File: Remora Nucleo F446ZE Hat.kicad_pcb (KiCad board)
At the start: 2 copper layers, 108.2 x 137.1 mm, 30 parts, among them J1 NucleoF446ZE CN11 Header, J10 B_STEP_AND_DIR+-, J11 C_STEP_AND_DIR+-, J12 DIGITAL_OUTPUTS, J14 Digital Inputs, J2 NucleoF446ZE CN12 Header, J3 UART_TX, J4 MSD-1-A, J6 X_STEP_AND_DIR+-, J7 Y_STEP_AND_DIR+-, J8 Z_STEP_AND_DIR+-, J9 A_STEP_AND_DIR+-, SW2 SW_Push

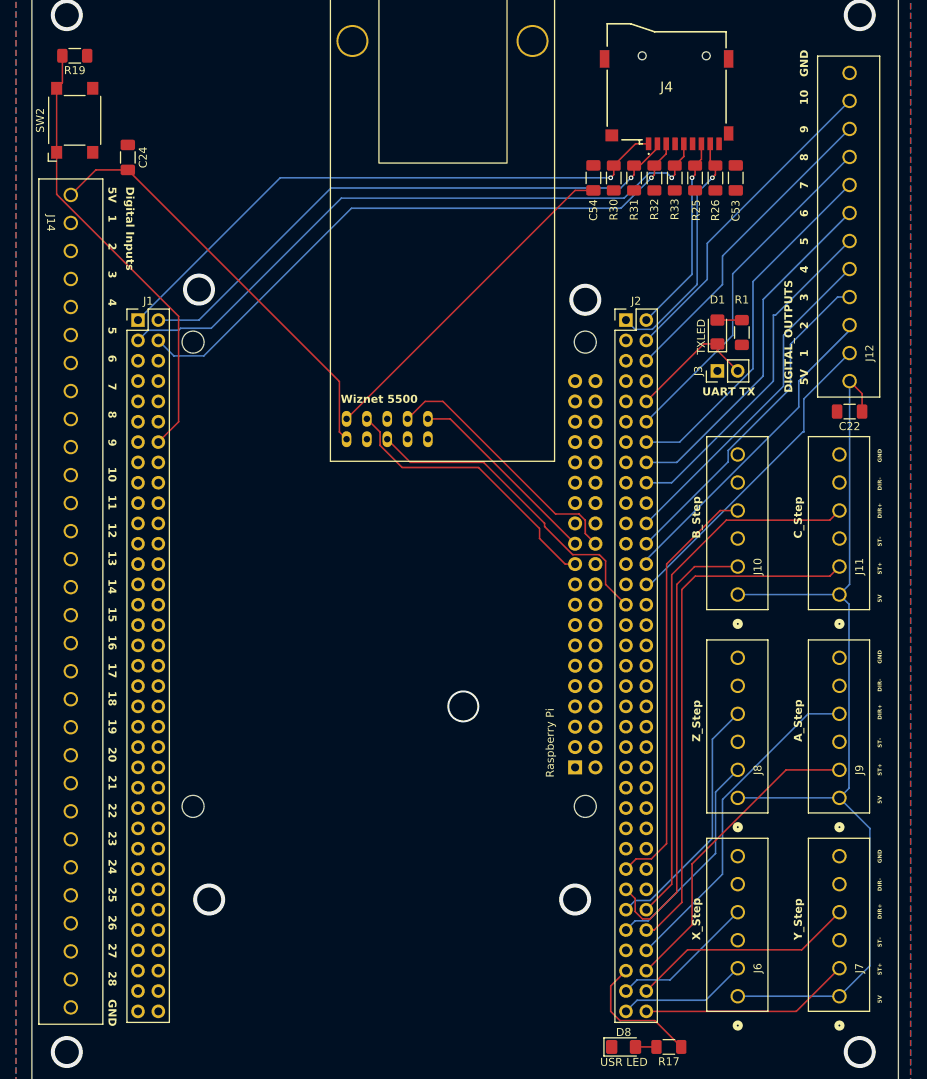
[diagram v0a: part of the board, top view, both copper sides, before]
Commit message: Dropped number of IO on design to make more room. Created the new footprints to suit them, updates to BOM and ran some traces on the PCB.
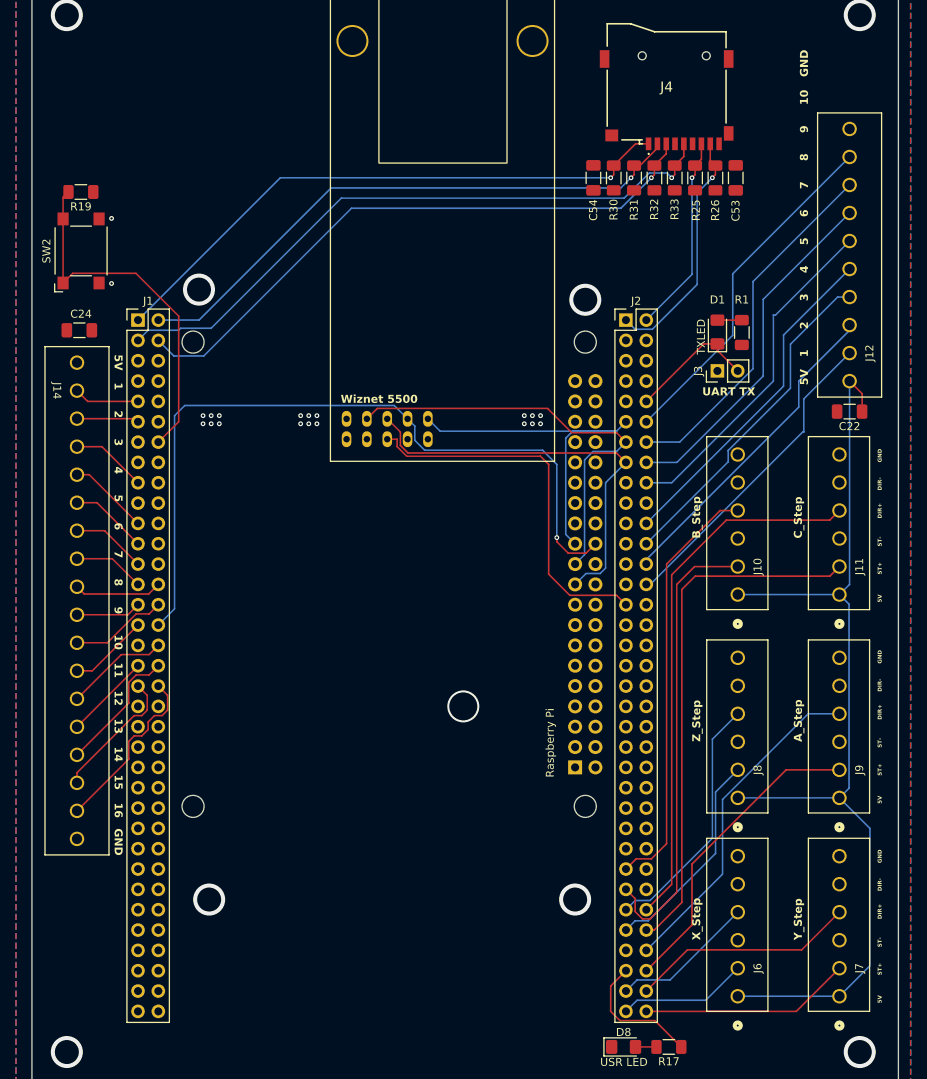
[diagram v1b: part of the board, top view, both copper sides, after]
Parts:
- J12: footprint EBWA_06_A:CONN_EBWA-12-A_ADM -> EBWA_06_A:CONN_EBWA-10-A_ADM
- J14: footprint EBWA_06_A:CONN_EBWA-30-A_ADM -> EBWA_06_A:CONN_EBWA-18-A_ADM
- moved C24 22.4 mm to (99.4, 67.3), turned to 0 degrees
- moved J14 21.0 mm to (99.1, 71.4)
- moved R19 17.0 mm to (99.5, 50.0)
- moved SW2 16.3 mm to (99.6, 57.4)
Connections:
- J1 pad 39: MCU_DIGITAL_IN_17 -> unconnected-(J1-Pin_39-Pad39)
- J1 pad 40: MCU_DIGITAL_IN_18 -> unconnected-(J1-Pin_40-Pad40)
- J1 pad 41: MCU_DIGITAL_IN_19 -> unconnected-(J1-Pin_41-Pad41)
- J1 pad 42: MCU_DIGITAL_IN_20 -> unconnected-(J1-Pin_42-Pad42)
- J1 pad 43: MCU_DIGITAL_IN_21 -> unconnected-(J1-Pin_43-Pad43)
- J1 pad 44: MCU_DIGITAL_IN_22 -> unconnected-(J1-Pin_44-Pad44)
- J1 pad 45: MCU_DIGITAL_IN_23 -> unconnected-(J1-Pin_45-Pad45)
- J1 pad 46: MCU_DIGITAL_IN_24 -> unconnected-(J1-Pin_46-Pad46)
- J1 pad 47: MCU_DIGITAL_IN_25 -> unconnected-(J1-Pin_47-Pad47)
- J1 pad 48: MCU_DIGITAL_IN_26 -> unconnected-(J1-Pin_48-Pad48)
- J1 pad 50: MCU_DIGITAL_IN_28 -> unconnected-(J1-Pin_50-Pad50)
- J1 pad 51: MCU_DIGITAL_IN_27 -> unconnected-(J1-Pin_51-Pad51)
- J12 pad 10: MCU_DIGITAL_OUT_9 -> GNDREF
- J14 pad 18: MCU_DIGITAL_IN_17 -> GNDREF
- J2 pad 4: MCU_DIGITAL_OUT_10 -> unconnected-(J2-Pin_4-Pad4)
- J2 pad 6: MCU_DIGITAL_OUT_9 -> unconnected-(J2-Pin_6-Pad6)
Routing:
- net /SPI1_CS: track 32.7 -> 94.9 mm, vias 0 -> 1
- net +5VD: track 177.5 -> 124.1 mm
- net /SPI1_MOSI: track 0.00 -> 52.0 mm
- net +3V3: track 42.7 -> 0.00 mm
- net MCU_DIGITAL_OUT_10: track 40.4 -> 0.00 mm
- net MCU_DIGITAL_OUT_9: track 39.5 -> 0.00 mm
- net MCU_DIGITAL_IN_16: track 0.00 -> 21.9 mm
- net /SPI1_CLK: track 24.9 -> 46.3 mm
- net /SPI1_MISO: track 35.2 -> 54.2 mm
- net MCU_DIGITAL_IN_15: track 0.00 -> 16.8 mm
- net MCU_DIGITAL_IN_14: track 0.00 -> 16.3 mm
- net MCU_DIGITAL_IN_12: track 0.00 -> 12.9 mm
- net MCU_DIGITAL_IN_10: track 0.00 -> 12.1 mm
- net MCU_DIGITAL_IN_8: track 0.00 -> 11.0 mm
- net MCU_DIGITAL_IN_13: track 0.00 -> 10.8 mm
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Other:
- board text removed: "17"
- board text removed: "18"
- board text removed: "19"
- board text removed: "20"
- board text removed: "21"
- board text removed: "22"
- board text removed: "23"
- board text removed: "24"
- board text removed: "25"
- board text removed: "26"
- board text removed: "27"
- board text removed: "28"

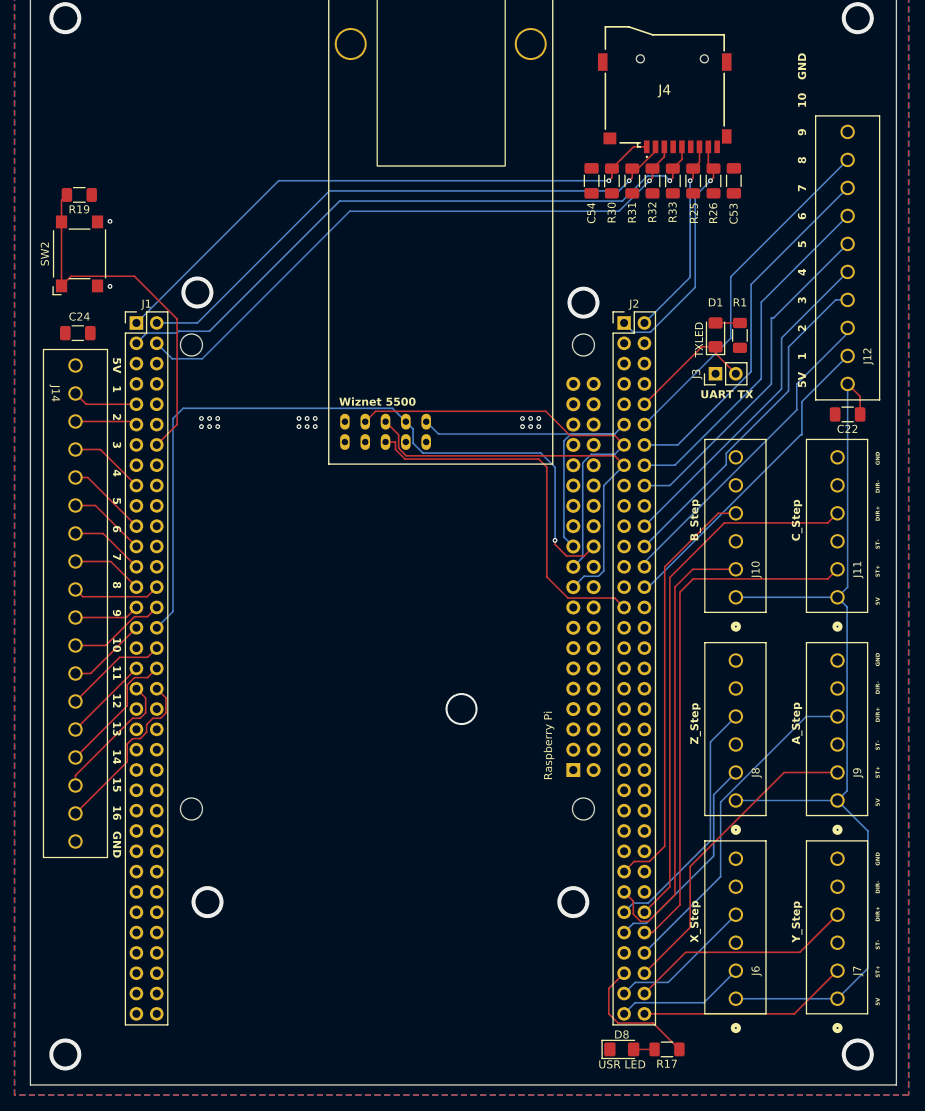
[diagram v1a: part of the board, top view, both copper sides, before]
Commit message: New optocoupler part choice, removed digikey BOM as have started inputting them into symbol fields. Re-enabled all disabled parts for now and will re-design power supplies soon.
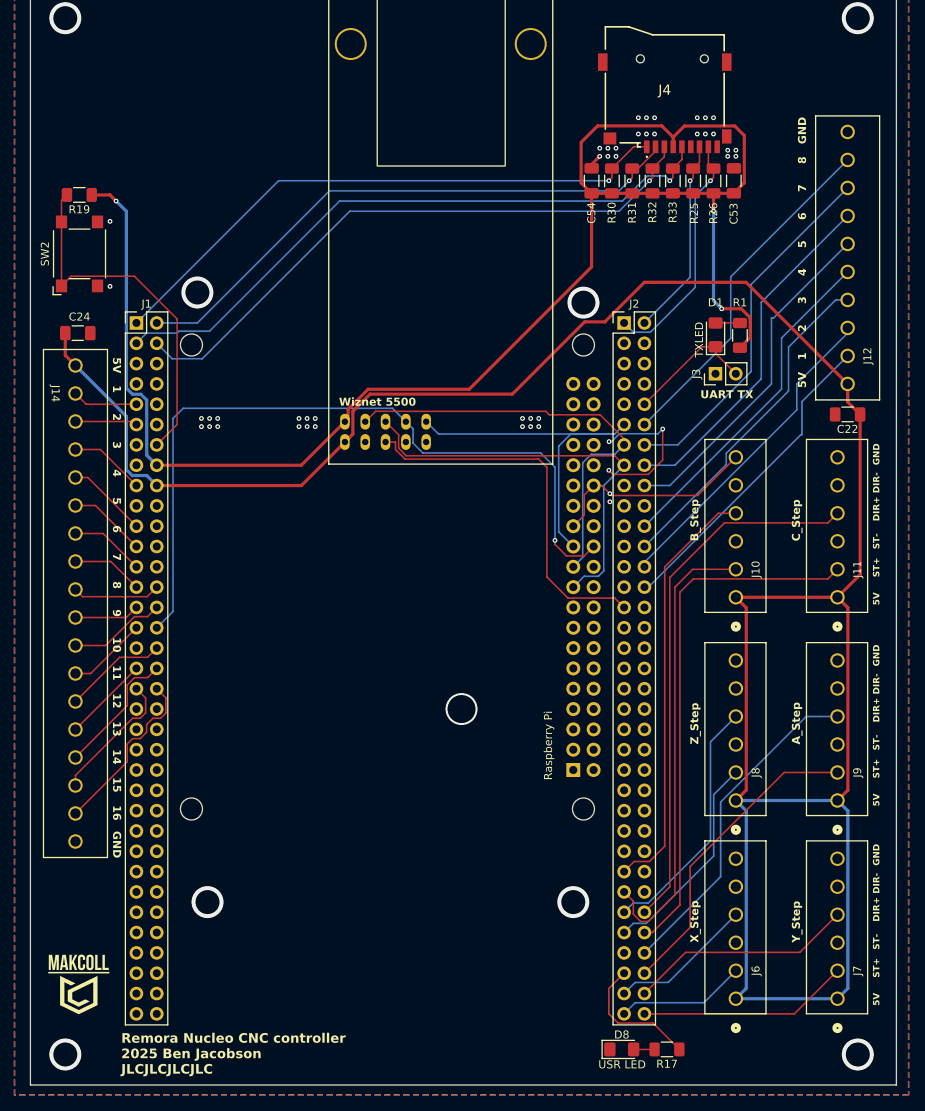
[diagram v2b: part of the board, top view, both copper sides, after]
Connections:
- J1 pad 16: unconnected-(J1-Pin_16-Pad16) -> +3V3
- J1 pad 18: unconnected-(J1-Pin_18-Pad18) -> +5VD
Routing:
- net +3V3: track 0.00 -> 193.5 mm, vias 0 -> 3
- net +5VD: track 124.1 -> 299.9 mm
- net GNDREF: track 0.41 -> 47.7 mm, vias 29 -> 56
- net /SPI1_CLK: track 46.3 -> 46.8 mm
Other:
- board text added: "Remora Nucleo CNC controller 2025 Ben Jacobson JLCJLCJLCJLC"

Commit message: BOM consolidation for various resistors. Moved BOM into symbol libraries and updated supplimentary BOM. Switched IO optical isolation circuitry to a more cost effective part.
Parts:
- removed the J12 at (195.6, 73.7)
- added C10: 100nF, Capacitor_SMD:C_1206_3216Metric_Pad1.33x1.80mm_HandSolder, F.Cu at (23.6, 78.3)
- added C11: 100nF, Capacitor_SMD:C_1206_3216Metric_Pad1.33x1.80mm_HandSolder, F.Cu at (23.6, 81.7)
- added C12: 100nF, Capacitor_SMD:C_1206_3216Metric_Pad1.33x1.80mm_HandSolder, F.Cu at (23.6, 85.0)
- added C13: 100nF, Capacitor_SMD:C_1206_3216Metric_Pad1.33x1.80mm_HandSolder, F.Cu at (44.7, 75.0)
- added C14: 100nF, Capacitor_SMD:C_1206_3216Metric_Pad1.33x1.80mm_HandSolder, F.Cu at (44.7, 78.3)
- added C15: 100nF, Capacitor_SMD:C_1206_3216Metric_Pad1.33x1.80mm_HandSolder, F.Cu at (44.7, 81.7)
- added C16: 100nF, Capacitor_SMD:C_1206_3216Metric_Pad1.33x1.80mm_HandSolder, F.Cu at (44.7, 85.0)
- added C17: 100nF, Capacitor_SMD:C_1206_3216Metric_Pad1.33x1.80mm_HandSolder, F.Cu at (23.6, 96.8)
- added C18: 100nF, Capacitor_SMD:C_1206_3216Metric_Pad1.33x1.80mm_HandSolder, F.Cu at (23.6, 100.1)
- added C19: 100nF, Capacitor_SMD:C_1206_3216Metric_Pad1.33x1.80mm_HandSolder, F.Cu at (23.6, 103.5)
- added C20: 100nF, Capacitor_SMD:C_1206_3216Metric_Pad1.33x1.80mm_HandSolder, F.Cu at (23.6, 106.8)
- added C9: 100nF, Capacitor_SMD:C_1206_3216Metric_Pad1.33x1.80mm_HandSolder, F.Cu at (23.6, 75.0)
- added D5: 9VLED, Diode_SMD:D_1206_3216Metric_Pad1.42x1.75mm_HandSolder, F.Cu at (44.7, 105.7)
- added D6: 5VLED, Diode_SMD:D_1206_3216Metric_Pad1.42x1.75mm_HandSolder, F.Cu at (44.7, 109.1)
- added F1: PRG18BB330MB1RB, Fuse:Fuse_0603_1608Metric_Pad1.05x0.95mm_HandSolder, F.Cu at (60.1, 59.3)
- added F2: PRG18BB330MB1RB, Fuse:Fuse_0603_1608Metric_Pad1.05x0.95mm_HandSolder, F.Cu at (60.1, 61.8)
- added F3: PRG18BB330MB1RB, Fuse:Fuse_0603_1608Metric_Pad1.05x0.95mm_HandSolder, F.Cu at (60.1, 64.3)
- added F4: PRG18BB330MB1RB, Fuse:Fuse_0603_1608Metric_Pad1.05x0.95mm_HandSolder, F.Cu at (60.1, 66.8)
- added F5: PRG18BB330MB1RB, Fuse:Fuse_0603_1608Metric_Pad1.05x0.95mm_HandSolder, F.Cu at (38.3, 59.3)
- added F6: PRG18BB330MB1RB, Fuse:Fuse_0603_1608Metric_Pad1.05x0.95mm_HandSolder, F.Cu at (38.3, 61.8)
- added F7: PRG18BB330MB1RB, Fuse:Fuse_0603_1608Metric_Pad1.05x0.95mm_HandSolder, F.Cu at (38.3, 64.3)
- added F8: PRG18BB330MB1RB, Fuse:Fuse_0603_1608Metric_Pad1.05x0.95mm_HandSolder, F.Cu at (38.3, 66.8)
- added J13: DIGITAL_OUTPUTS, EBWA_06_A:CONN_EBWA-10-A_ADM, F.Cu at (195.3, 73.7)
- added J16: 5V External Power Inlet, EBWA_02_A:ADAMTECH_EBWA-02-A, F.Cu at (106.7, 31.5)
- added J17: 9V External Power Inlet, EBWA_02_A:ADAMTECH_EBWA-02-A, F.Cu at (117.6, 31.5)
- added R14: 360R, Resistor_SMD:R_1206_3216Metric_Pad1.30x1.75mm_HandSolder, F.Cu at (50.7, 105.7)
- added R15: 150R, Resistor_SMD:R_1206_3216Metric_Pad1.30x1.75mm_HandSolder, F.Cu at (50.7, 109.0)
- added R16: 120R, Resistor_SMD:R_1206_3216Metric_Pad1.30x1.75mm_HandSolder, F.Cu at (45.4, 59.7)
- added R17: 120R, Resistor_SMD:R_1206_3216Metric_Pad1.30x1.75mm_HandSolder, F.Cu at (45.4, 63.0)
- added R18: 120R, Resistor_SMD:R_1206_3216Metric_Pad1.30x1.75mm_HandSolder, F.Cu at (45.4, 66.3)
- added R19: 120R, Resistor_SMD:R_1206_3216Metric_Pad1.30x1.75mm_HandSolder, F.Cu at (45.4, 69.7)
- added R20: 120R, Resistor_SMD:R_1206_3216Metric_Pad1.30x1.75mm_HandSolder, F.Cu at (23.6, 59.7)
- added R21: 120R, Resistor_SMD:R_1206_3216Metric_Pad1.30x1.75mm_HandSolder, F.Cu at (23.6, 63.0)
- added R22: 120R, Resistor_SMD:R_1206_3216Metric_Pad1.30x1.75mm_HandSolder, F.Cu at (23.6, 66.3)
- added R23: 120R, Resistor_SMD:R_1206_3216Metric_Pad1.30x1.75mm_HandSolder, F.Cu at (23.6, 69.7)
- added R28: 180R, Resistor_SMD:R_1206_3216Metric_Pad1.30x1.75mm_HandSolder, F.Cu at (64.5, 96.8)
- added R29: 180R, Resistor_SMD:R_1206_3216Metric_Pad1.30x1.75mm_HandSolder, F.Cu at (64.5, 100.1)
- added R30: 180R, Resistor_SMD:R_1206_3216Metric_Pad1.30x1.75mm_HandSolder, F.Cu at (64.5, 103.4)
- added R31: 180R, Resistor_SMD:R_1206_3216Metric_Pad1.30x1.75mm_HandSolder, F.Cu at (64.5, 106.7)
- added R32: 180R, Resistor_SMD:R_1206_3216Metric_Pad1.30x1.75mm_HandSolder, F.Cu at (67.3, 59.7)
- added R33: 180R, Resistor_SMD:R_1206_3216Metric_Pad1.30x1.75mm_HandSolder, F.Cu at (67.3, 63.0)
- added R34: 180R, Resistor_SMD:R_1206_3216Metric_Pad1.30x1.75mm_HandSolder, F.Cu at (67.3, 66.3)
- added R35: 180R, Resistor_SMD:R_1206_3216Metric_Pad1.30x1.75mm_HandSolder, F.Cu at (67.3, 69.7)
- added R36: 180R, Resistor_SMD:R_1206_3216Metric_Pad1.30x1.75mm_HandSolder, F.Cu at (65.8, 75.0)
- added R37: 180R, Resistor_SMD:R_1206_3216Metric_Pad1.30x1.75mm_HandSolder, F.Cu at (65.8, 78.3)
- added R38: 180R, Resistor_SMD:R_1206_3216Metric_Pad1.30x1.75mm_HandSolder, F.Cu at (65.8, 81.6)
- added R39: 180R, Resistor_SMD:R_1206_3216Metric_Pad1.30x1.75mm_HandSolder, F.Cu at (65.8, 84.9)
- added R40: 180R, Resistor_SMD:R_1206_3216Metric_Pad1.30x1.75mm_HandSolder, F.Cu at (64.5, 112.0)
- added R41: 180R, Resistor_SMD:R_1206_3216Metric_Pad1.30x1.75mm_HandSolder, F.Cu at (64.5, 115.3)
- added R42: 180R, Resistor_SMD:R_1206_3216Metric_Pad1.30x1.75mm_HandSolder, F.Cu at (64.5, 118.6)
- added R43: 180R, Resistor_SMD:R_1206_3216Metric_Pad1.30x1.75mm_HandSolder, F.Cu at (64.5, 121.9)
- added U10: ADUM1201ARZ, Package_SO:SOIC-8_3.9x4.9mm_P1.27mm, F.Cu at (48.1, 143.3)
- added U11: HT26LS31ARZ, Package_DIP:SMDIP-4_W9.53mm, F.Cu at (52.9, 130.8)
- added U12: ADUM1201ARZ, Package_SO:SOIC-8_3.9x4.9mm_P1.27mm, F.Cu at (28.2, 157.5)
- added U13: ADUM1201ARZ, Package_SO:SOIC-8_3.9x4.9mm_P1.27mm, F.Cu at (22.9, 144.3)
- added U14: HT26LS31ARZ, Package_DIP:SMDIP-4_W9.53mm, F.Cu at (22.9, 131.8)
- added U19: LTV-247, Package_SO:SOP-16_4.4x10.4mm_P1.27mm, F.Cu at (75.0, 64.0)
- added U20: LTV-247, Package_SO:SOP-16_4.4x10.4mm_P1.27mm, F.Cu at (73.5, 79.3)
- added U21: LTV-247, Package_SO:SOP-16_4.4x10.4mm_P1.27mm, F.Cu at (71.4, 148.5)
- added U22: LTV-247, Package_SO:SOP-16_4.4x10.4mm_P1.27mm, F.Cu at (72.2, 101.1)
- added U4: ADUM1201ARZ, Package_SO:SOIC-8_3.9x4.9mm_P1.27mm, F.Cu at (61.2, 142.5)
- added U5: ADUM1201ARZ, Package_SO:SOIC-8_3.9x4.9mm_P1.27mm, F.Cu at (61.0, 150.9)
- added U6: HT26LS31ARZ, Package_DIP:SMDIP-4_W9.53mm, F.Cu at (37.7, 132.1)
- added U7: LTV-247, Package_SO:SOP-16_4.4x10.4mm_P1.27mm, F.Cu at (53.2, 64.0)
- added U8: LTV-247, Package_SO:SOP-16_4.4x10.4mm_P1.27mm, F.Cu at (31.3, 64.0)
- added U9: ADUM1201ARZ, Package_SO:SOIC-8_3.9x4.9mm_P1.27mm, F.Cu at (37.1, 144.0)
- renumbered C53 to C1, C54 to C2, C22 to C21, C24 to C23, D8 to D1, D1 to D2, J9 to J10, J10 to J11, J11 to J12, J14 to J15, J4 to J2, J2 to J4, J6 to J7, J7 to J8, J8 to J9, R19 to R1, R17 to R2, R1 to R3, R25 to R4, R26 to R5, R30 to R6, R31 to R7, R32 to R8, R33 to R9, SW2 to SW1
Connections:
- C21 pad 2: GNDREF -> GNDPWR
- C23 pad 2: GNDREF -> GNDPWR
- J1 pad 18: +5VD -> +5V
- J10 pad 2: /MCU_A_STEP -> /Z and A Stepper Drivers/A_STEP+
- J10 pad 3: unconnected-(J9-Pin_3-Pad3) -> /Z and A Stepper Drivers/A_STEP-
- J10 pad 4: /MCU_A_DIR -> /Z and A Stepper Drivers/A_DIR+
- J10 pad 5: unconnected-(J9-Pin_5-Pad5) -> /Z and A Stepper Drivers/A_DIR-
- J10 pad 6: GNDREF -> GNDPWR
- J11 pad 2: /MCU_B_STEP -> /B and C Stepper Drivers/B_STEP+
- J11 pad 3: unconnected-(J10-Pin_3-Pad3) -> /B and C Stepper Drivers/B_STEP-
- J11 pad 4: /MCU_B_DIR -> /B and C Stepper Drivers/B_DIR+
- J11 pad 5: unconnected-(J10-Pin_5-Pad5) -> /B and C Stepper Drivers/B_DIR-
- J11 pad 6: GNDREF -> GNDPWR
- J12 pad 2: /MCU_C_STEP -> /B and C Stepper Drivers/C_STEP+
- J12 pad 3: unconnected-(J11-Pin_3-Pad3) -> /B and C Stepper Drivers/C_STEP-
- J12 pad 4: /MCU_C_DIR -> /B and C Stepper Drivers/C_DIR+
- J12 pad 5: unconnected-(J11-Pin_5-Pad5) -> /B and C Stepper Drivers/C_DIR-
- J12 pad 6: GNDREF -> GNDPWR
- J15 pad 10: MCU_DIGITAL_IN_9 -> /Digital Inputs/Digital Input 9-12/INPUT9
- J15 pad 11: MCU_DIGITAL_IN_10 -> /Digital Inputs/Digital Input 9-12/INPUT10
- J15 pad 12: MCU_DIGITAL_IN_11 -> /Digital Inputs/Digital Input 9-12/INPUT11
- J15 pad 13: MCU_DIGITAL_IN_12 -> /Digital Inputs/Digital Input 9-12/INPUT12
- J15 pad 14: MCU_DIGITAL_IN_13 -> /Digital Inputs/Digital Input 13-16/INPUT13
- J15 pad 15: MCU_DIGITAL_IN_14 -> /Digital Inputs/Digital Input 13-16/INPUT14
- J15 pad 16: MCU_DIGITAL_IN_15 -> /Digital Inputs/Digital Input 13-16/INPUT15
- J15 pad 17: MCU_DIGITAL_IN_16 -> /Digital Inputs/Digital Input 13-16/INPUT16
- J15 pad 18: GNDREF -> GNDPWR
- J15 pad 2: MCU_DIGITAL_IN_1 -> /Digital Inputs/Digital Input 1-4/INPUT1
- J15 pad 3: MCU_DIGITAL_IN_2 -> /Digital Inputs/Digital Input 1-4/INPUT2
- J15 pad 4: MCU_DIGITAL_IN_3 -> /Digital Inputs/Digital Input 1-4/INPUT3
- J15 pad 5: MCU_DIGITAL_IN_4 -> /Digital Inputs/Digital Input 1-4/INPUT4
- J15 pad 6: MCU_DIGITAL_IN_5 -> /Digital Inputs/Digital Input 5-8/INPUT5
- J15 pad 7: MCU_DIGITAL_IN_6 -> /Digital Inputs/Digital Input 5-8/INPUT6
- J15 pad 8: MCU_DIGITAL_IN_7 -> /Digital Inputs/Digital Input 5-8/INPUT7
- J15 pad 9: MCU_DIGITAL_IN_8 -> /Digital Inputs/Digital Input 5-8/INPUT8
- J7 pad 2: /MCU_X_STEP -> /X and Y Stepper Drivers/X_STEP+
- J7 pad 3: unconnected-(J6-Pin_3-Pad3) -> /X and Y Stepper Drivers/X_STEP-
- J7 pad 4: /MCU_X_DIR -> /X and Y Stepper Drivers/X_DIR+
- J7 pad 5: unconnected-(J6-Pin_5-Pad5) -> /X and Y Stepper Drivers/X_DIR-
- J7 pad 6: GNDREF -> GNDPWR
- J8 pad 2: /MCU_Y_STEP -> /X and Y Stepper Drivers/Y_STEP+
- J8 pad 3: unconnected-(J7-Pin_3-Pad3) -> /X and Y Stepper Drivers/Y_STEP-
- J8 pad 4: /MCU_Y_DIR -> /X and Y Stepper Drivers/Y_DIR+
- J8 pad 5: unconnected-(J7-Pin_5-Pad5) -> /X and Y Stepper Drivers/Y_DIR-
- J8 pad 6: GNDREF -> GNDPWR
- J9 pad 2: /MCU_Z_STEP -> /Z and A Stepper Drivers/Z_STEP+
- J9 pad 3: unconnected-(J8-Pin_3-Pad3) -> /Z and A Stepper Drivers/Z_STEP-
- J9 pad 4: /MCU_Z_DIR -> /Z and A Stepper Drivers/Z_DIR+
- J9 pad 5: unconnected-(J8-Pin_5-Pad5) -> /Z and A Stepper Drivers/Z_DIR-
- J9 pad 6: GNDREF -> GNDPWR
- U1 pad 6: +5VD -> +5V
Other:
- board text added: "INPUTS"
- board text added: "OUTPUTS"
- board text added: "Remora Nucleo CNC controller V1"
- board text added: "© 2025 Ben Jacobson JLCJLCJLCJLC"
- board text removed: "Remora Nucleo CNC controller 2025 Ben Jacobson JLCJLCJLCJLC"
